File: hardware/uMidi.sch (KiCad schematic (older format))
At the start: 61 parts, among them CON1 USB-MINI-B, IC1 ATXMEGA128A4U-M, IC2 74LS14, IC3 LT1129CST-3.3, IC4 6N138, P1 MIDI In, P2 MIDI Thru, P3 MIDI T/O, P4 MIDI Out, P5 5..12 V, P6 PDI, P7 GPIO1, P8 GPIO2, P9 GPIO3

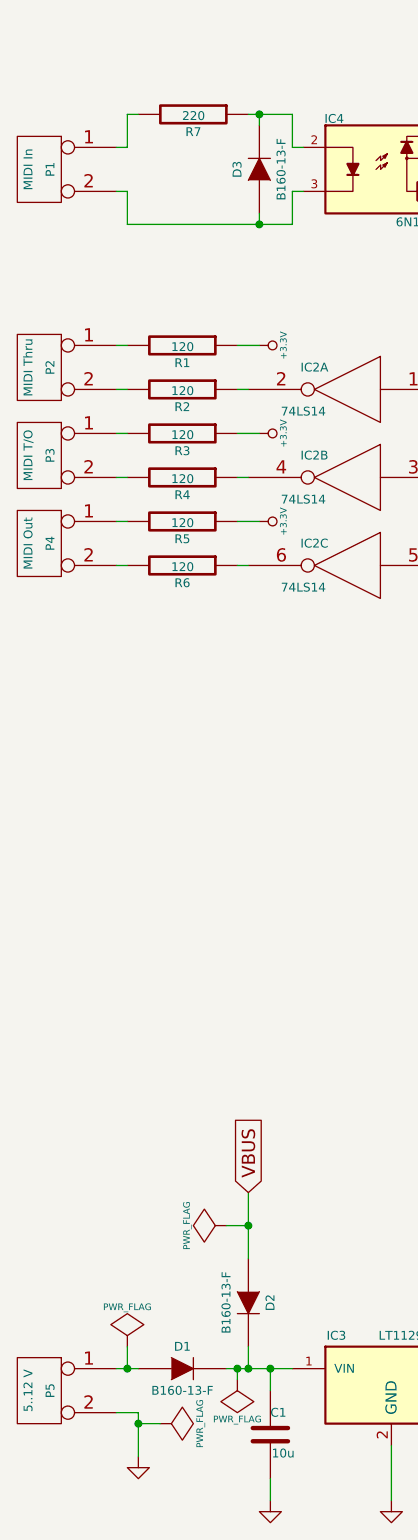
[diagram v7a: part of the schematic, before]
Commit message: Assign footprints in schematic
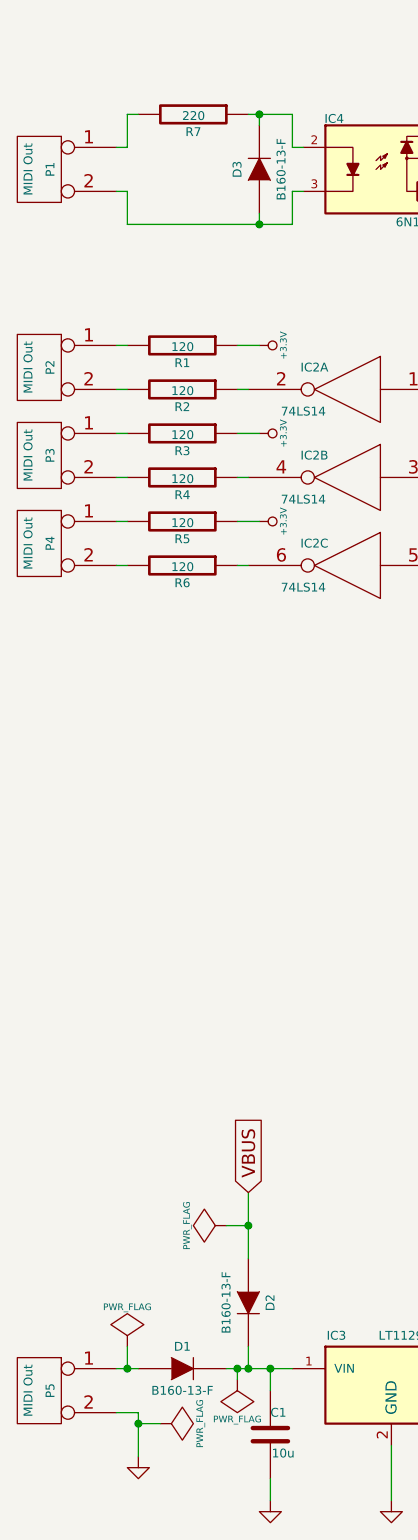
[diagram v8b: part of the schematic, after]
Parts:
- C6: footprint (none) -> Capacitors_SMD:C_0603
- CON1: footprint (none) -> uMIDI:USB-mini-B-UX60MB-5ST
- D1, D2, D3: footprint SMD:DI-214-AC_SMA -> uMIDI:DO-214-AC_SMA
- IC1: footprint Atmel:QFN-44-1EP -> uMIDI:QFN-44-1EP
- IC2: footprint (none) -> uMIDI:SOIC-14_N
- IC4: footprint Opto:Optocoupler_DIP8_SMD -> uMIDI:Optocoupler_DIP8_SMD
- JP1: footprint (none) -> uMIDI:SJ3
- JP2, JP3, JP4, JP5: footprint (none) -> uMIDI:SJ2
- P1: value MIDI In -> MIDI Out; footprint (none) -> uMIDI:Pinhead1-2
- P2: value MIDI Thru -> MIDI Out; footprint (none) -> uMIDI:Pinhead1-2
- P3: value MIDI T/O -> MIDI Out; footprint (none) -> uMIDI:Pinhead1-2
- P4: footprint (none) -> uMIDI:Pinhead1-2
- P5: value 5..12 V -> MIDI Out; footprint (none) -> uMIDI:Pinhead1-2
- P6: footprint (none) -> Pin_Headers:Pin_Header_Straight_2x03
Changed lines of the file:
@@
 F 0 "IC1" H 7750 4750 40  0000 L BNN
 F 1 "ATXMEGA128A4U-M" H 8850 2300 40  0000 L BNN
-F 2 "Atmel:QFN-44-1EP" H 8500 3550 35  0001 C CIN
+F 2 "uMIDI:QFN-44-1EP" H 8500 3550 35  0001 C CIN
 F 3 "http://www.atmel.com/images/Atmel-8387-8-and16-bit-AVR-Microcontroller-XMEGA-A4U_Datasheet.pdf" H 8500 3550 60  0001 C CNN
 F 4 "Digikey" H 7750 4750 40  0001 L BNN "Supplier"
@@
 F 0 "P6" V 6600 2400 60  0000 C CNN
 F 1 "PDI" V 6700 2400 60  0000 C CNN
-F 2 "" H 6650 2400 60  0001 C CNN
+F 2 "Pin_Headers:Pin_Header_Straight_2x03" H 6650 2400 60  0001 C CNN
 F 3 "http://portal.fciconnect.com/Comergent//fci/drawing/67996.pdf" H 6650 2400 60  0001 C CNN
 F 4 "609-3210-ND" V 6600 2400 60  0001 C CNN "Supplier Part Number"
@@
 F 0 "IC2" H 3300 3200 40  0000 C CNN
 F 1 "74LS14" H 3350 3000 40  0000 C CNN
-F 2 "" H 3150 3100 60  0001 C CNN
+F 2 "uMIDI:SOIC-14_N" H 3150 3100 60  0001 C CNN
 F 3 "http://www.nxp.com/documents/data_sheet/74LVT14.pdf" H 3150 3100 60  0001 C CNN
 F 4 "568-8193-1-ND" H 3300 3200 40  0001 C CNN "Supplier Part Number"
@@
 F 0 "IC2" H 2350 2400 40  0000 C CNN
 F 1 "74LS14" H 2400 2200 40  0000 C CNN
-F 2 "" H 2200 2300 60  0001 C CNN
+F 2 "uMIDI:SOIC-14_N" H 2200 2300 60  0001 C CNN
 F 3 "http://www.nxp.com/documents/data_sheet/74LVT14.pdf" H 2200 2300 60  0001 C CNN
 F 4 "568-8193-1-ND" H 2350 2400 40  0001 C CNN "Supplier Part Number"
@@
 F 0 "IC2" H 2350 2800 40  0000 C CNN
 F 1 "74LS14" H 2400 2600 40  0000 C CNN
-F 2 "" H 2200 2700 60  0001 C CNN
+F 2 "uMIDI:SOIC-14_N" H 2200 2700 60  0001 C CNN
 F 3 "http://www.nxp.com/documents/data_sheet/74LVT14.pdf" H 2200 2700 60  0001 C CNN
 F 4 "568-8193-1-ND" H 2350 2800 40  0001 C CNN "Supplier Part Number"
@@
 F 0 "IC2" H 3300 2800 40  0000 C CNN
 F 1 "74LS14" H 3350 2600 40  0000 C CNN
-F 2 "" H 3150 2700 60  0001 C CNN
+F 2 "uMIDI:SOIC-14_N" H 3150 2700 60  0001 C CNN
 F 3 "http://www.nxp.com/documents/data_sheet/74LVT14.pdf" H 3150 2700 60  0001 C CNN
 F 4 "568-8193-1-ND" H 3300 2800 40  0001 C CNN "Supplier Part Number"
@@
 F 0 "IC2" H 3300 2400 40  0000 C CNN
 F 1 "74LS14" H 3350 2200 40  0000 C CNN
-F 2 "" H 3150 2300 60  0001 C CNN
+F 2 "uMIDI:SOIC-14_N" H 3150 2300 60  0001 C CNN
 F 3 "http://www.nxp.com/documents/data_sheet/74LVT14.pdf" H 3150 2300 60  0001 C CNN
 F 4 "568-8193-1-ND" H 3300 2400 40  0001 C CNN "Supplier Part Number"
@@
 F 0 "IC2" H 2350 3200 40  0000 C CNN
 F 1 "74LS14" H 2400 3000 40  0000 C CNN
-F 2 "" H 2200 3100 60  0001 C CNN
+F 2 "uMIDI:SOIC-14_N" H 2200 3100 60  0001 C CNN
 F 3 "http://www.nxp.com/documents/data_sheet/74LVT14.pdf" H 2200 3100 60  0001 C CNN
 F 4 "568-8193-1-ND" H 2350 3200 40  0001 C CNN "Supplier Part Number"
@@
 F 0 "CON1" H 5200 4950 60  0000 C CNN
 F 1 "USB-MINI-B" H 4950 4250 60  0000 C CNN
-F 2 "" H 4950 4600 60  0001 C CNN
+F 2 "uMIDI:USB-mini-B-UX60MB-5ST" H 4950 4600 60  0001 C CNN
 F 3 "https://www.hirose.com/product/en/download_file/key_name/UX60SC%2DMB%2D5ST%2801%29/category/Specification%20Sheet/doc_file_id/36416/?file_category_id=9&item_id=02400016601&is_series=" H 4950 4600 60  0001 C CNN
 F 4 "H2959CT-ND" H 5200 4950 60  0001 C CNN "Supplier Part Number"
@@
 F 0 "JP1" H 3800 2600 40  0000 L CNN
 F 1 "JUMPER3" H 3750 2800 40  0000 C CNN
-F 2 "" H 3750 2700 60  0001 C CNN
+F 2 "uMIDI:SJ3" H 3750 2700 60  0001 C CNN
 F 3 "" H 3750 2700 60  0001 C CNN
 	1    3750 2700
@@
 F 0 "P4" V 750 3000 40  0000 C CNN
 F 1 "MIDI Out" V 850 3000 40  0000 C CNN
-F 2 "" H 800 3000 60  0001 C CNN
+F 2 "uMIDI:Pinhead1-2" H 800 3000 60  0001 C CNN
 F 3 "" H 800 3000 60  0001 C CNN
 	1    800  3000
@@
 P 800 2200
 F 0 "P2" V 750 2200 40  0000 C CNN
-F 1 "MIDI Thru" V 850 2200 40  0000 C CNN
-F 2 "" H 800 2200 60  0001 C CNN
+F 1 "MIDI Out" V 850 2200 40  0000 C CNN
+F 2 "uMIDI:Pinhead1-2" H 800 2200 60  0001 C CNN
 F 3 "" H 800 2200 60  0001 C CNN
 	1    800  2200
@@
 P 800 2600
 F 0 "P3" V 750 2600 40  0000 C CNN
-F 1 "MIDI T/O" V 850 2600 40  0000 C CNN
-F 2 "" H 800 2600 60  0001 C CNN
+F 1 "MIDI Out" V 850 2600 40  0000 C CNN
+F 2 "uMIDI:Pinhead1-2" H 800 2600 60  0001 C CNN
 F 3 "" H 800 2600 60  0001 C CNN
 	1    800  2600
@@
 F 0 "IC4" H 2140 1530 40  0000 C CNN
 F 1 "6N138" H 2510 1060 40  0000 C CNN
-F 2 "Opto:Optocoupler_DIP8_SMD" H 2150 1070 30  0001 C CIN
+F 2 "uMIDI:Optocoupler_DIP8_SMD" H 2150 1070 30  0001 C CIN
 F 3 "" H 2350 1300 60  0001 C CNN
 F 4 "Lite-On Inc." H 2140 1530 40  0001 C CNN "Manufacturer"
@@
 F 0 "D3" H 1800 1400 40  0000 C CNN
 F 1 "B160-13-F" H 1800 1200 40  0000 C CNN
-F 2 "SMD:DI-214-AC_SMA" H 1800 1300 60  0001 C CNN
+F 2 "uMIDI:DO-214-AC_SMA" H 1800 1300 60  0001 C CNN
 F 3 "http://www.diodes.com/_files/datasheets/ds13002.pdf" H 1800 1300 60  0001 C CNN
 F 4 "https://www.digikey.de/product-detail/de/B160-13-F/B160-FDICT-ND/806561" H 1800 1400 40  0001 C CNN "Supplier Link"
@@
 P 800 1300
 F 0 "P1" V 750 1300 40  0000 C CNN
-F 1 "MIDI In" V 850 1300 40  0000 C CNN
-F 2 "" H 800 1300 60  0001 C CNN
+F 1 "MIDI Out" V 850 1300 40  0000 C CNN
+F 2 "uMIDI:Pinhead1-2" H 800 1300 60  0001 C CNN
 F 3 "" H 800 1300 60  0001 C CNN
 	1    800  1300
@@
 F 0 "D2" H 1750 6550 40  0000 C CNN
 F 1 "B160-13-F" H 1750 6350 40  0000 C CNN
-F 2 "SMD:DI-214-AC_SMA" H 1750 6450 60  0001 C CNN
+F 2 "uMIDI:DO-214-AC_SMA" H 1750 6450 60  0001 C CNN
 F 3 "http://www.diodes.com/_files/datasheets/ds13002.pdf" H 1750 6450 60  0001 C CNN
 F 4 "Diodes Incorporated" H 1750 6550 40  0001 C CNN "Manufacturer"
@@
 F 0 "D1" H 1450 6850 40  0000 C CNN
 F 1 "B160-13-F" H 1450 6650 40  0000 C CNN
-F 2 "SMD:DI-214-AC_SMA" H 1450 6750 60  0001 C CNN
+F 2 "uMIDI:DO-214-AC_SMA" H 1450 6750 60  0001 C CNN
 F 3 "http://www.diodes.com/_files/datasheets/ds13002.pdf" H 1450 6750 60  0001 C CNN
 F 4 "Diodes Incorporated" H 1450 6850 40  0001 C CNN "Manufacturer"
@@
 P 800 6850
 F 0 "P5" V 750 6850 40  0000 C CNN
-F 1 "5..12 V" V 850 6850 40  0000 C CNN
-F 2 "" H 800 6850 60  0001 C CNN
+F 1 "MIDI Out" V 850 6850 40  0000 C CNN
+F 2 "uMIDI:Pinhead1-2" H 800 6850 60  0001 C CNN
 F 3 "" H 800 6850 60  0001 C CNN
 	1    800  6850
@@
 F 0 "C6" V 4850 5300 40  0000 L CNN
 F 1 "4.7n" V 5150 5300 40  0000 L CNN
-F 2 "" H 5038 5200 30  0001 C CNN
+F 2 "Capacitors_SMD:C_0603" H 5038 5200 30  0001 C CNN
 F 3 "" H 5000 5350 60  0001 C CNN
 F 4 "490-1506-1-ND" V 4850 5300 40  0001 L CNN "Supplier Part Number"
@@
 F 0 "JP2" H 5300 3000 60  0000 C CNN
 F 1 "JUMPER" H 5300 2770 40  0000 C CNN
-F 2 "" H 5300 2850 60  0001 C CNN
+F 2 "uMIDI:SJ2" H 5300 2850 60  0001 C CNN
 F 3 "" H 5300 2850 60  0001 C CNN
 	1    5300 2850
@@
 F 0 "JP3" H 5300 3300 60  0000 C CNN
 F 1 "JUMPER" H 5300 3070 40  0000 C CNN
-F 2 "" H 5300 3150 60  0001 C CNN
+F 2 "uMIDI:SJ2" H 5300 3150 60  0001 C CNN
 F 3 "" H 5300 3150 60  0001 C CNN
 	1    5300 3150
@@
 F 0 "JP4" H 5300 3600 60  0000 C CNN
 F 1 "JUMPER" H 5300 3370 40  0000 C CNN
-F 2 "" H 5300 3450 60  0001 C CNN
+F 2 "uMIDI:SJ2" H 5300 3450 60  0001 C CNN
 F 3 "" H 5300 3450 60  0001 C CNN
 	1    5300 3450
@@
 F 0 "JP5" H 5300 3900 60  0000 C CNN
 F 1 "JUMPER" H 5300 3670 40  0000 C CNN
-F 2 "" H 5300 3750 60  0001 C CNN
+F 2 "uMIDI:SJ2" H 5300 3750 60  0001 C CNN
 F 3 "" H 5300 3750 60  0001 C CNN
 	1    5300 3750
